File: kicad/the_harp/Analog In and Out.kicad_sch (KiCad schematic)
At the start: 26 parts, among them U701 OPA2365AIDR, U702 OPA1688IDR

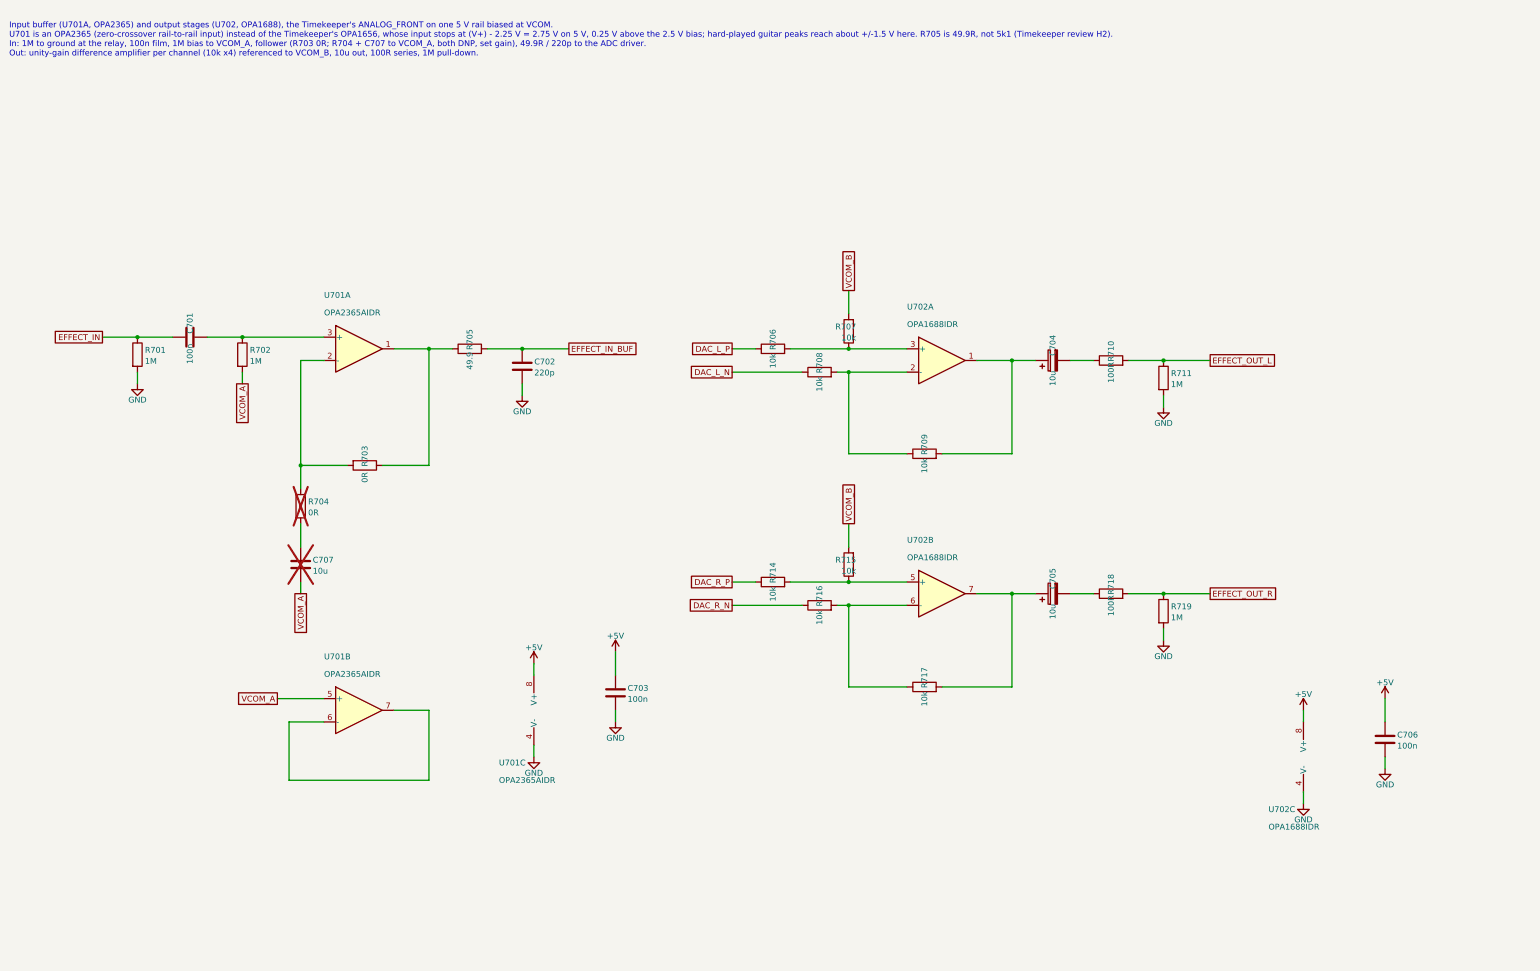
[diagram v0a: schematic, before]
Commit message: Stereo single-ended input and an OLED display
IN becomes a TRS jack (tip left, ring right) with a second OPA2365 buffer and
THS4522 channel B into the AK4621EF's AINR; the codec inputs are no longer
parked. A mono plug is detected by the right channel reading silence. The
twelve note LEDs and R107-R118 give way to a 0.91 in I2C OLED connector (J408,
PB6/PB7) with 4.7k pull-ups. Schematic regenerated (190 parts, netlist OK on
all sheets); design brief, PCB plan, firmware requirements and the design
report updated. The PCB still carries the old LED footprints until Update PCB
from Schematic is run in KiCad.

Co-Authored-By: Claude Sonnet 5.5 <noreply@anthropic.com>
Claude-Session: https://claude.ai/code/session_016hDejPHPgG8auBLMyByYZK
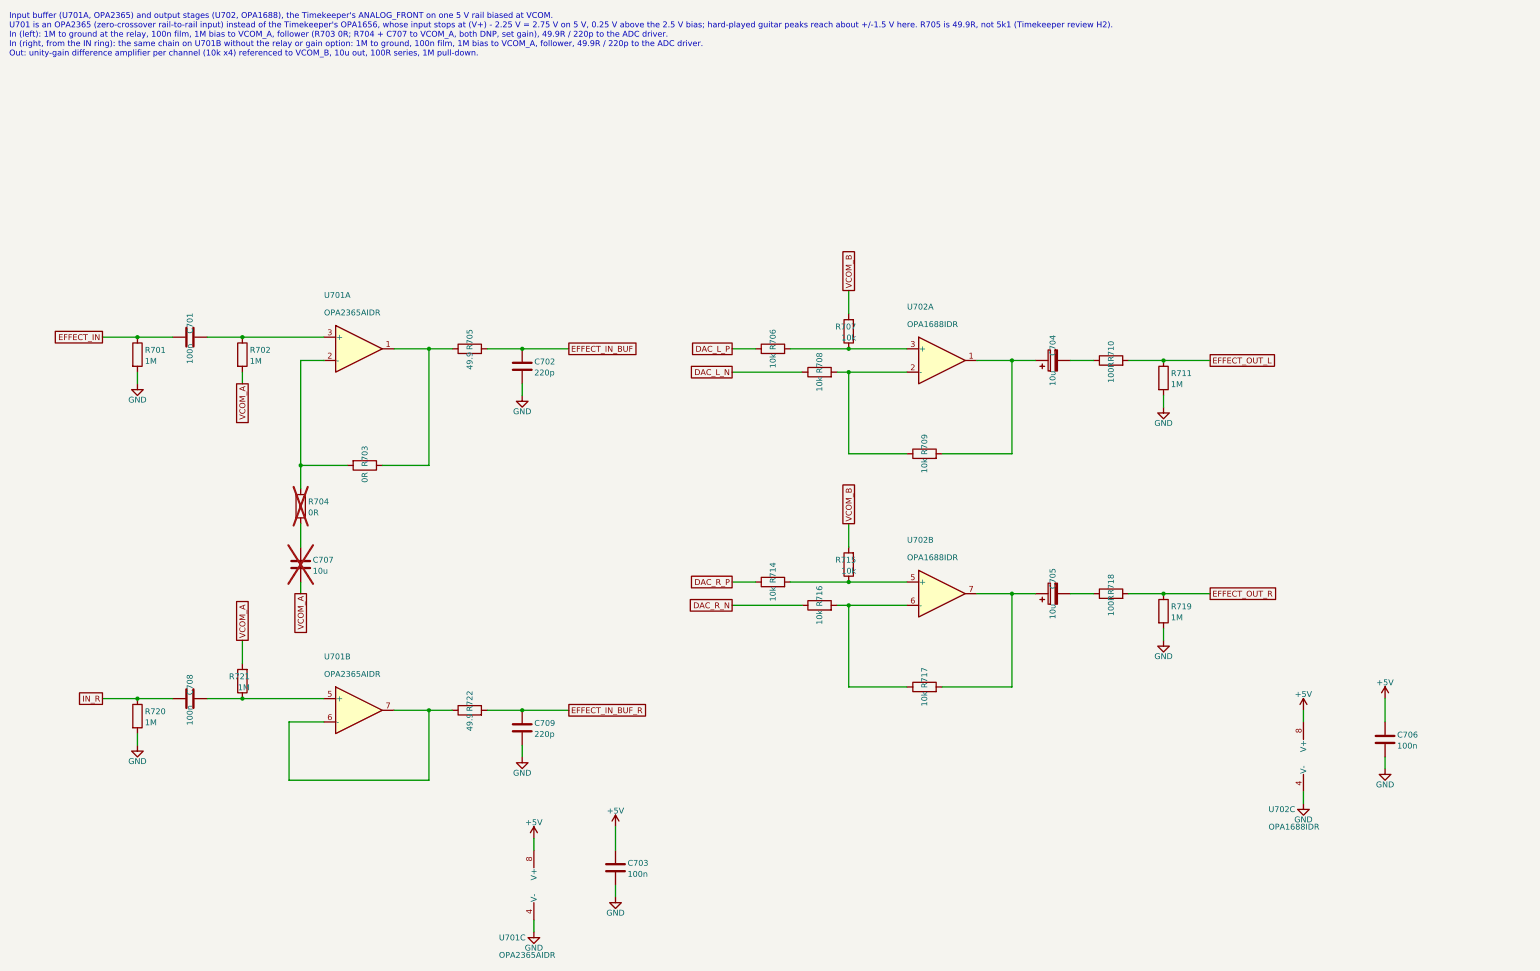
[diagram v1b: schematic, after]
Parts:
- added C708: 100n, Capacitor_SMD:C_1206_3216Metric, symbol Device:C
- added C709: 220p, Capacitor_SMD:C_0603_1608Metric, symbol Device:C
- added R720, R721: 1M, Resistor_SMD:R_0603_1608Metric, symbol Device:R
- added R722: 49.9, Resistor_SMD:R_0603_1608Metric, symbol Device:R
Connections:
- net GND: now also C709.2, R720.2
- net VCOM_A: now also R721.2; no longer U701.5 (+)
- net at U701.6 (-), U701.7: now also R722.1
- new net: C708.2, R721.1, U701.5 (+)
- new net EFFECT_IN_BUF_R: C709.1, R722.2
- new net IN_R: C708.1, R720.1
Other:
- moved on the sheet: C703, U701C
